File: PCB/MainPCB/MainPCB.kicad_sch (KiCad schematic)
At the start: 59 parts, among them J10 JST-XH, J11 JST-XH, J13 JST-XH, J14 JST-XH, J15 JST-XH, J2 JST-XH, J3 JST-XH, J3 XT30PW-M, J5 JST-XH, J6 JST-XH, J7 JST-XH, J8 JST-XH, J9 JST-XH, Q1 MTB7D0N6RJ3, Q2 MTB7D0N6RJ3, Q3 TJ60S04M3L, SW1 SW_Push, SW2 SW_DPST_x2, U1 Pico, U15 AZ1117CH-3.3TR, U2 MCP1401T-E_OT, U3 MCP1401T-E_OT

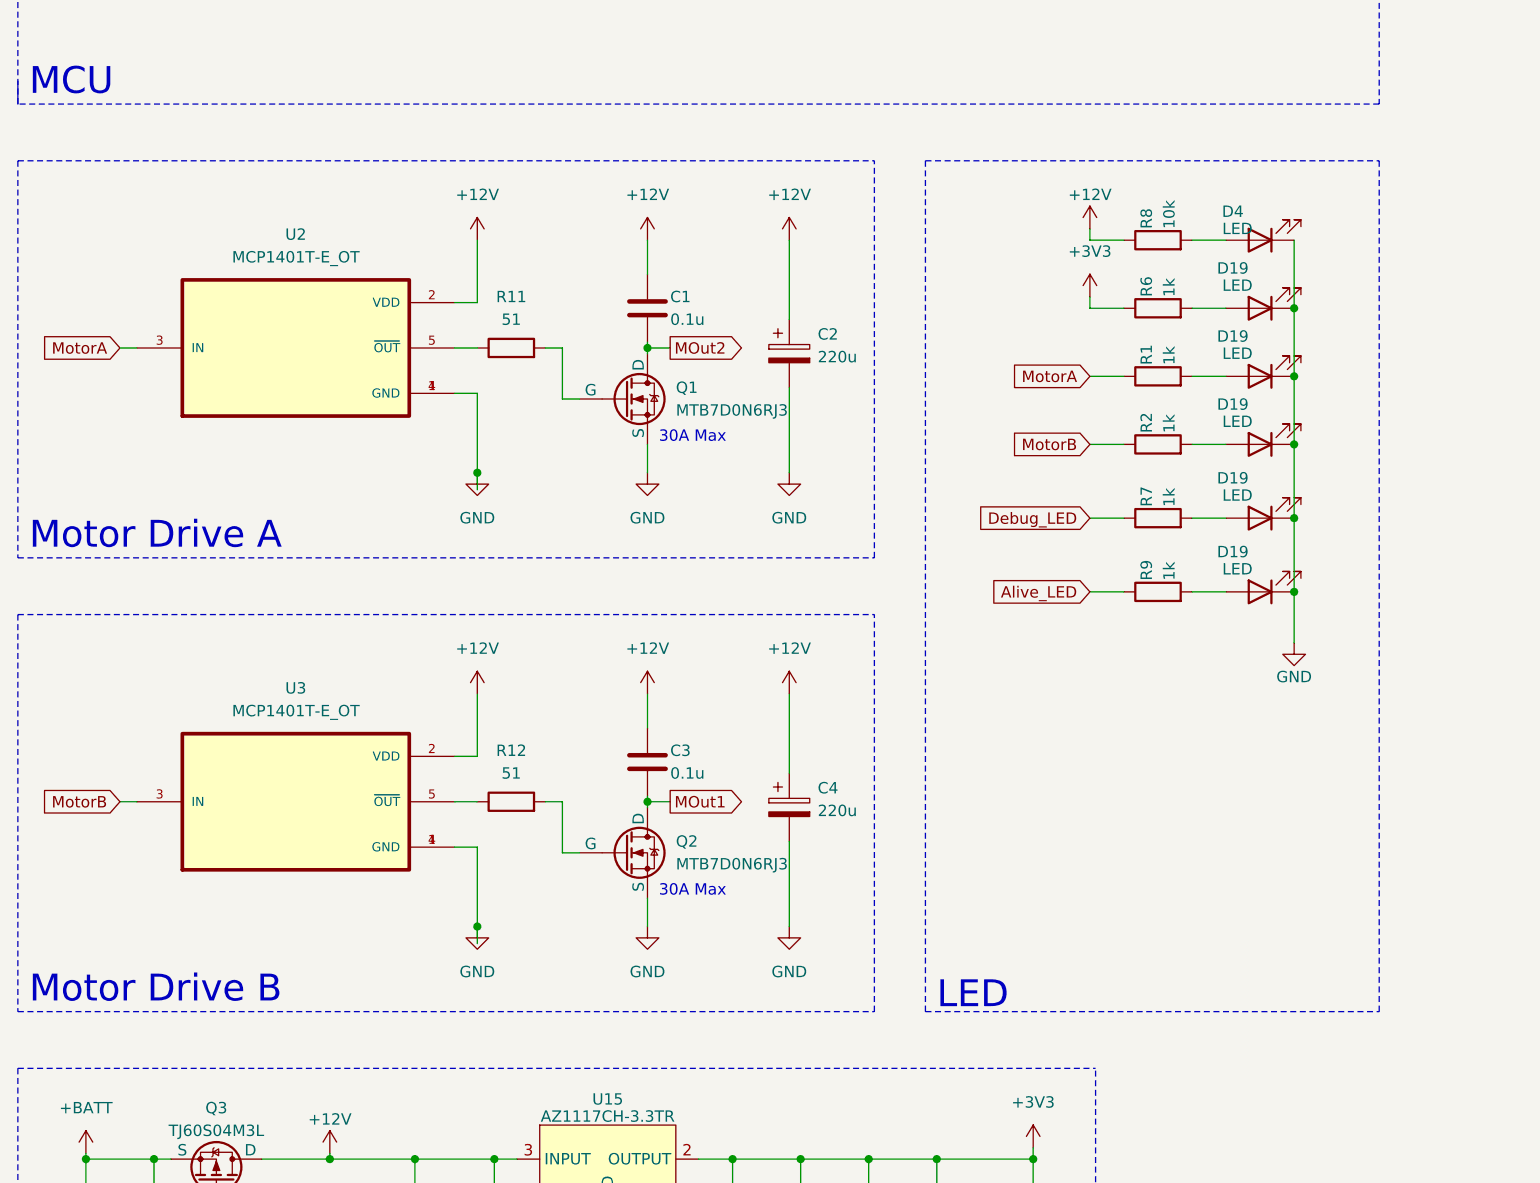
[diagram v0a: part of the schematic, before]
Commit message: :sparkles: フリーホイールダイオードを追加
# ==== Emojis ====
# ✨ :sparkles: Add new feature
# ✅  :white_check_mark: Update existing feature (not bug)
# ⚠️  :warning: Fix bug/error
# 🔥  :fire: Remove files or features
# ✏️ :pencil2: Fix typos
# 📝  :memo: Update documentation
# ♻️  :recycle: Dependencies update
# 🐧  :penguin: Improved the Linux
# 🍎  :apple: Improved the macOS
# 🔖 :bookmark: Add new library
# 🎉  :tada: Initial commit

# ==== Format ====
# :emoji: Subject
#
# Commit body...

# ==== Messages ====
# 新規(ファイル)機能追加: Add
# 機能修正、既存機能追加（バグではない): Update
# リファクタリング: Clean
# ファイル名変更:
# 削除など: Remove
# バグ修正: Fix
# バージョンアップ: Upgrade
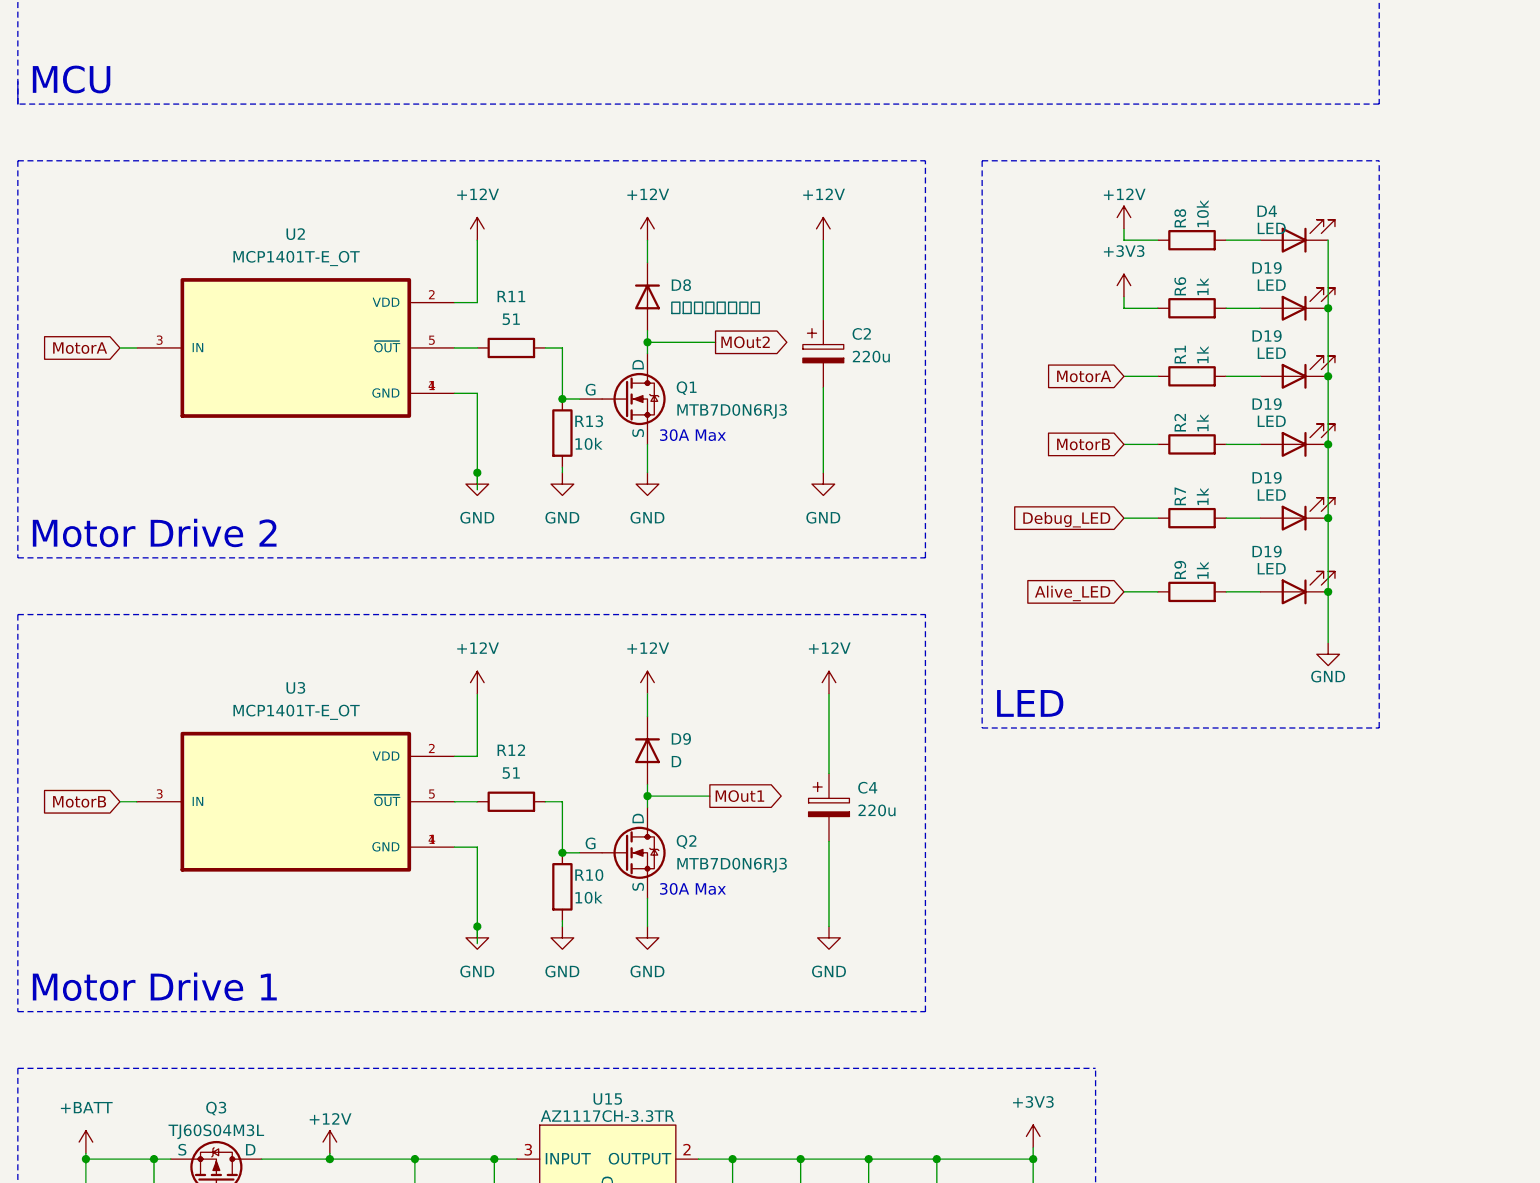
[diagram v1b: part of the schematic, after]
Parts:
- removed C1, C3: 0.1u, Capacitor_SMD:C_0603_1608Metric_Pad1.08x0.95mm_HandSolder, symbol Device:C
- added D8: ＧＳ１０１０ＦＬ, Diode_SMD:D_SOD-123F, symbol Device:D
- added D9: D, Diode_SMD:D_SOD-123F, symbol Device:D
- added R10, R13: 10k, Resistor_SMD:R_0603_1608Metric_Pad0.98x0.95mm_HandSolder, symbol Device:R
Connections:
- net +12V: now also D8.1 (K), D9.1 (K)
- net GND: now also R10.2, R13.2
- net MOut1: now also D9.2 (A)
- net MOut2: now also D8.2 (A)
- net at Q1.1 (G), R11.2: now also R13.1
- net at Q2.1 (G), R12.2: now also R10.1
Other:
- note added: "Motor Drive 1"
- note added: "Motor Drive 2"
- note removed: "Motor Drive A"
- note removed: "Motor Drive B"
- company: (none) -> Daiki Tomioka
- title: (none) -> Fried Rice Maker Charhan!!
- moved on the sheet: C2, C4, D19, D4, R1, R2, R6, R7, R8, R9

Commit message: :sparkles: Add PCB Production files
# ==== Emojis ====
# ✨ :sparkles: Add new feature
# ✅  :white_check_mark: Update existing feature (not bug)
# ⚠️  :warning: Fix bug/error
# 🔥  :fire: Remove files or features
# ✏️ :pencil2: Fix typos
# 📝  :memo: Update documentation
# ♻️  :recycle: Dependencies update
# 🐧  :penguin: Improved the Linux
# 🍎  :apple: Improved the macOS
# 🔖 :bookmark: Add new library
# 🎉  :tada: Initial commit

# ==== Format ====
# :emoji: Subject
#
# Commit body...

# ==== Messages ====
# 新規(ファイル)機能追加: Add
# 機能修正、既存機能追加（バグではない): Update
# リファクタリング: Clean
# ファイル名変更:
# 削除など: Remove
# バグ修正: Fix
# バージョンアップ: Upgrade
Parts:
- D9: value D -> ＧＳ１０１０ＦＬ
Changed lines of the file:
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@@
       (effects (font (size 1.27 1.27)) (justify left))
     )
-    (property "Value" "D" (at 92.075 194.31 90)
+    (property "Value" "ＧＳ１０１０ＦＬ" (at 92.075 194.31 90)
       (effects (font (size 1.27 1.27)) (justify left))
     )
